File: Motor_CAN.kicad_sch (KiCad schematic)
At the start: 20 parts, among them J20 MotorCANConnector, J27 CAN_TP, J5 M_CAN_IN, J7 M_CAN_OUT, U14 ADM3055E, U15 CDSOT23-T24CAN

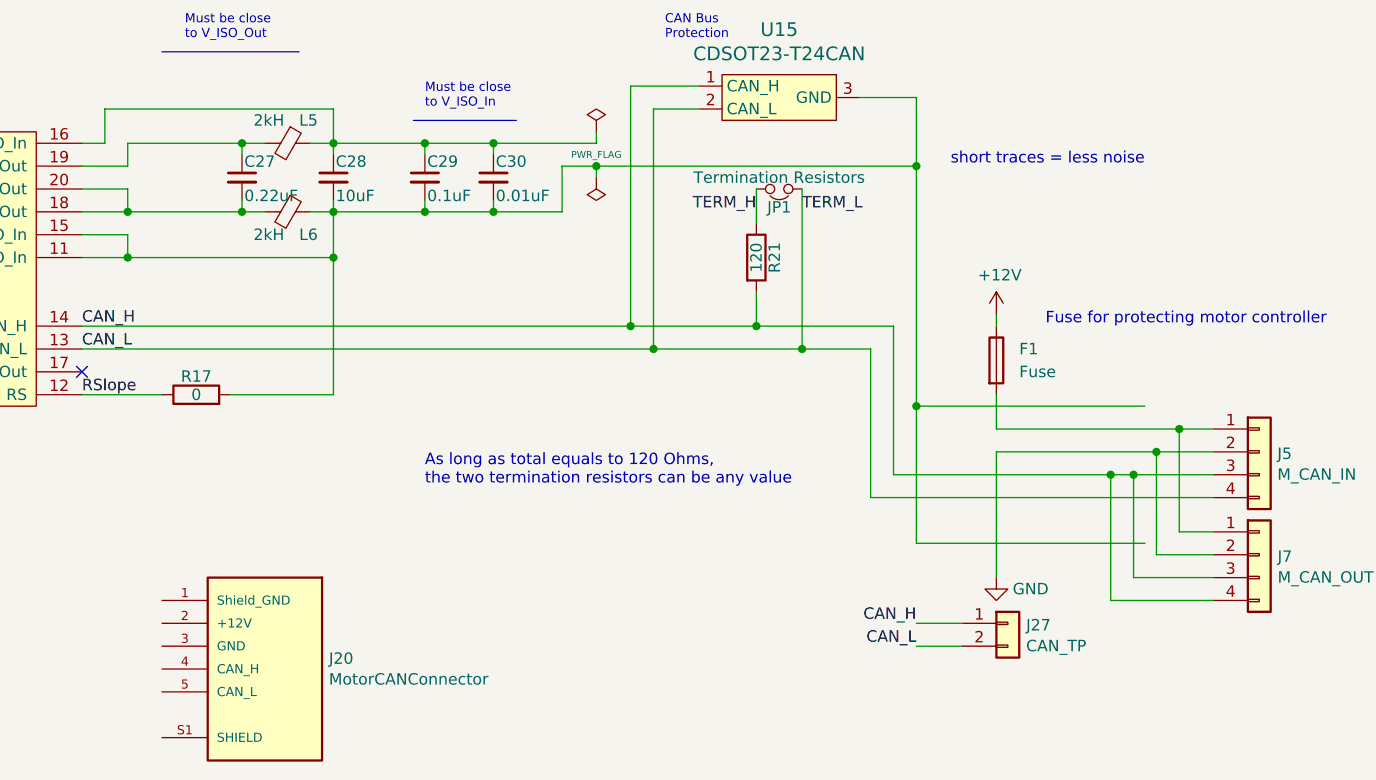
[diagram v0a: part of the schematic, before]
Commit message: Changed names and added power flags until KiCAD ERC was satisfied. Hopefully this did not involve doing anything that wasn't supposed to be done.
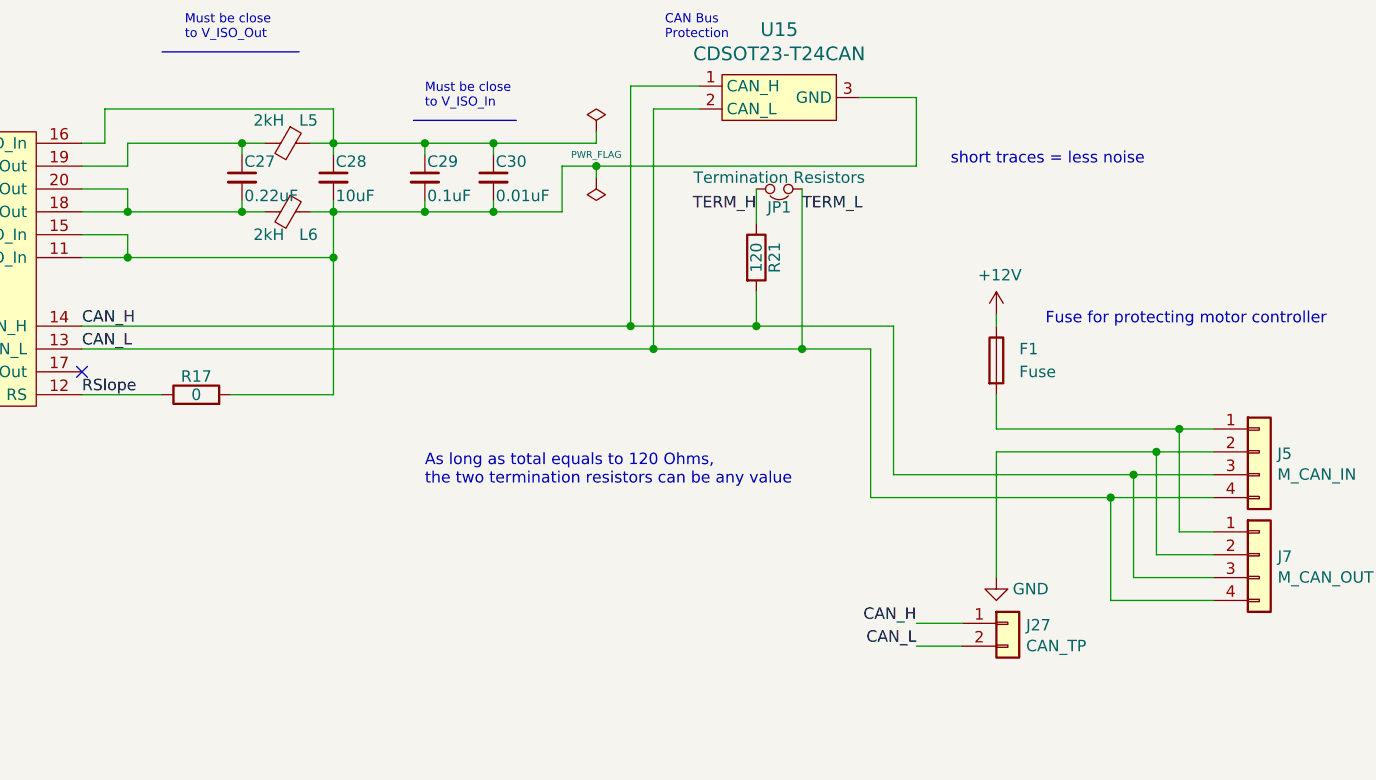
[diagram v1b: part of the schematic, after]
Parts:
- removed J20: MotorCANConnector, UTSVT_Connectors:TE_4-2172079-2, symbol Dashboard:MotorCANConnector-utsvt-connectors
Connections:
- net CAN_H: no longer J7.4 (Pin_4)
- net CAN_L: now also J7.4 (Pin_4)
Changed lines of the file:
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@@
 	)
 	(junction
-		(at 219.71 83.82)
+		(at 241.3 120.65)
 		(diameter 0)
 		(color 0 0 0 0)
@@
 	)
 	(junction
-		(at 241.3 118.11)
-		(diameter 0)
-		(color 0 0 0 0)
-	)
-	(junction
 		(at 154.94 93.98)
 		(diameter 0)
@@
 	)
 	(junction
-		(at 219.71 110.49)
-		(diameter 0)
-		(color 0 0 0 0)
-	)
-	(junction
 		(at 187.96 101.6)
 		(diameter 0)
@@
 	(wire
 		(pts
+			(xy 241.3 120.65) (xy 252.73 120.65)
+		)
+		(stroke
+			(width 0)
+			(type default)
+		)
+	)
+	(wire
+		(pts
 			(xy 187.96 101.6) (xy 201.93 101.6)
 		)
@@
 	(wire
 		(pts
-			(xy 219.71 110.49) (xy 245.11 110.49)
-		)
-		(stroke
-			(width 0)
-			(type default)
-		)
-	)
-	(wire
-		(pts
 			(xy 246.38 115.57) (xy 252.73 115.57)
 		)
@@
 		)
 	)
-	(wire
-		(pts
-			(xy 219.71 125.73) (xy 245.11 125.73)
-		)
-		(stroke
-			(width 0)
-			(type default)
-		)
-	)
 	(polyline
 		(pts
@@
 	(wire
 		(pts
-			(xy 219.71 83.82) (xy 219.71 110.49)
-		)
-		(stroke
-			(width 0)
-			(type default)
-		)
-	)
-	(wire
-		(pts
 			(xy 228.6 109.22) (xy 228.6 113.03)
 		)
@@
 	(wire
 		(pts
-			(xy 217.17 118.11) (xy 241.3 118.11)
+			(xy 217.17 118.11) (xy 243.84 118.11)
 		)
 		(stroke
@@
 	(wire
 		(pts
-			(xy 241.3 118.11) (xy 243.84 118.11)
-		)
-		(stroke
-			(width 0)
-			(type default)
-		)
-	)
-	(wire
-		(pts
 			(xy 154.94 77.47) (xy 154.94 81.28)
 		)
@@
 	(wire
 		(pts
+			(xy 241.3 120.65) (xy 241.3 132.08)
+		)
+		(stroke
+			(width 0)
+			(type default)
+		)
+	)
+	(wire
+		(pts
 			(xy 90.17 92.71) (xy 91.44 92.71)
 		)
@@
 	(wire
 		(pts
-			(xy 241.3 132.08) (xy 241.3 118.11)
-		)
-		(stroke
-			(width 0)
-			(type default)
-		)
-	)
-	(wire
-		(pts
 			(xy 82.55 85.09) (xy 82.55 86.36)
 		)
@@
 	(wire
 		(pts
-			(xy 219.71 110.49) (xy 219.71 125.73)
-		)
-		(stroke
-			(width 0)
-			(type default)
-		)
-	)
-	(wire
-		(pts
 			(xy 132.08 93.98) (xy 154.94 93.98)
 		)
@@
 	(wire
 		(pts
-			(xy 214.63 120.65) (xy 252.73 120.65)
+			(xy 214.63 120.65) (xy 241.3 120.65)
 		)
 		(stroke
@@
 					(unit 1)
 				)
-			)
-		)
-	)
-	(symbol
-		(lib_id "Dashboard:MotorCANConnector-utsvt-connectors")
-		(at 143.51 152.4 0)
-		(mirror y)
-		(unit 1)
-		(exclude_from_sim no)
-		(in_bom yes)
-		(on_board yes)
-		(dnp no)
-		(property "Reference" "J20"
-			(at 154.432 138.5316 0)
-			(effects
-				(font
-					(size 1.27 1.27)
-				)
-				(justify right)
-			)
-		)
-		(property "Value" "MotorCANConnector"
-			(at 154.432 140.843 0)
-			(effects
-				(font
-					(size 1.27 1.27)
-				)
-				(justify right)
-			)
-		)
-		(property "Footprint" "UTSVT_Connectors:TE_4-2172079-2"
-			(at 143.51 152.4 0)
-			(effects
-				(font
-					(size 1.27 1.27)
-				)
-				(hide yes)
-			)
-		)
-		(property "Datasheet" ""
-			(at 143.51 152.4 0)
-			(effects
-				(font
-					(size 1.27 1.27)
-				)
-				(hide yes)
-			)
-		)
-		(property "Description" ""
-			(at 143.51 152.4 0)
-			(effects
-				(font
-					(size 1.27 1.27)
-				)
-				(hide yes)
-			)
-		)
-		(property "Digikey" "https://www.digikey.com/product-detail/en/te-connectivity-amp-connectors/4-2172079-2/A120861-ND/5118755"
-			(at 143.51 152.4 0)
-			(effects
-				(font
-					(size 1.27 1.27)
-				)
-				(hide yes)
-			)
-		)
-		(pin "1"
-		)
-		(pin "2"
-		)
-		(pin "3"
-		)
-		(pin "4"
-		)
-		(pin "5"
-		)
-		(pin "S1"
-		)
-		(instances
-			(project "Controls-Leader"
-				(path "/66218487-e316-4467-9eba-79d4626ab24e/00000000-0000-0000-0000-00005f6018fb"
-					(reference "J20")
-					(unit 1)
-				)

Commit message: Fuse footprint added and blinker changed to software
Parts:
- F1: footprint (none) -> Fuse:Fuse_1206_3216Metric
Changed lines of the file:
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@@
 			)
 		)
-		(property "Footprint" ""
+		(property "Footprint" "Fuse:Fuse_1206_3216Metric"
 			(at 226.822 105.41 90)
 			(effects
@@
 			)
 		)
-		(property "Datasheet" "~"
+		(property "Datasheet" "https://www.littelfuse.com/~/media/electronics/datasheets/fuses/littelfuse_fuse_437_datasheet.pdf.pdf"
 			(at 228.6 105.41 0)
 			(effects

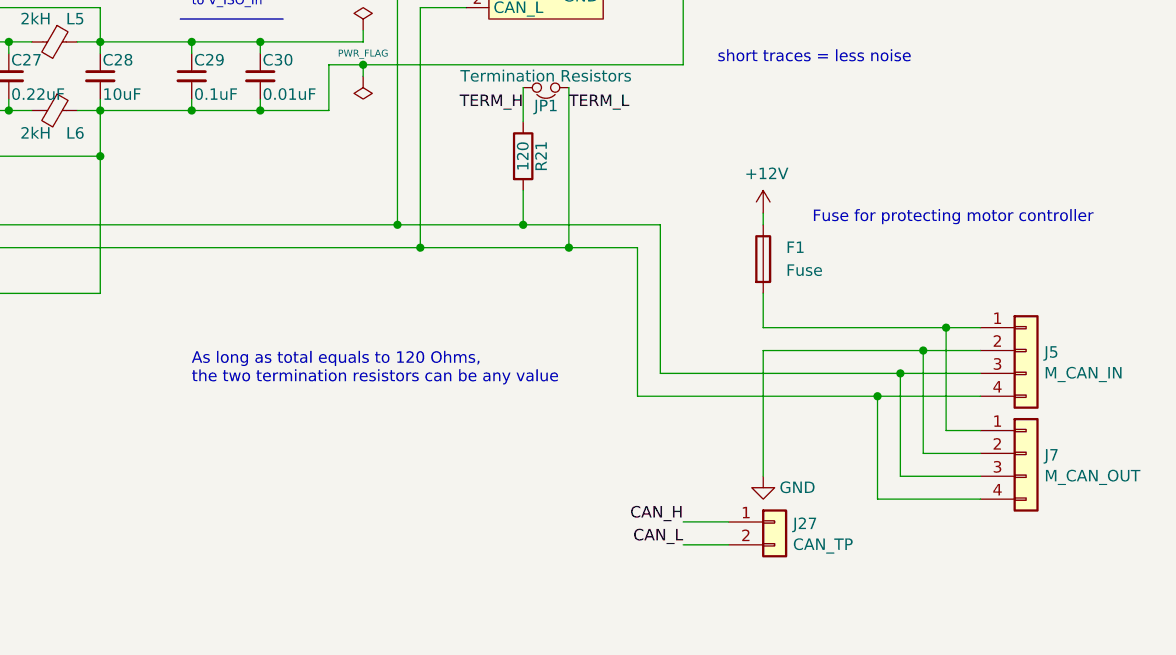
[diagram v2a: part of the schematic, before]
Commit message: Started cleaning some comments, changed EL3H7 data sheet link, removed extra motor CAN connector and changed original one to match (I think) motor controller connector, removed extra mounting holes, removed hierarchical power labels.
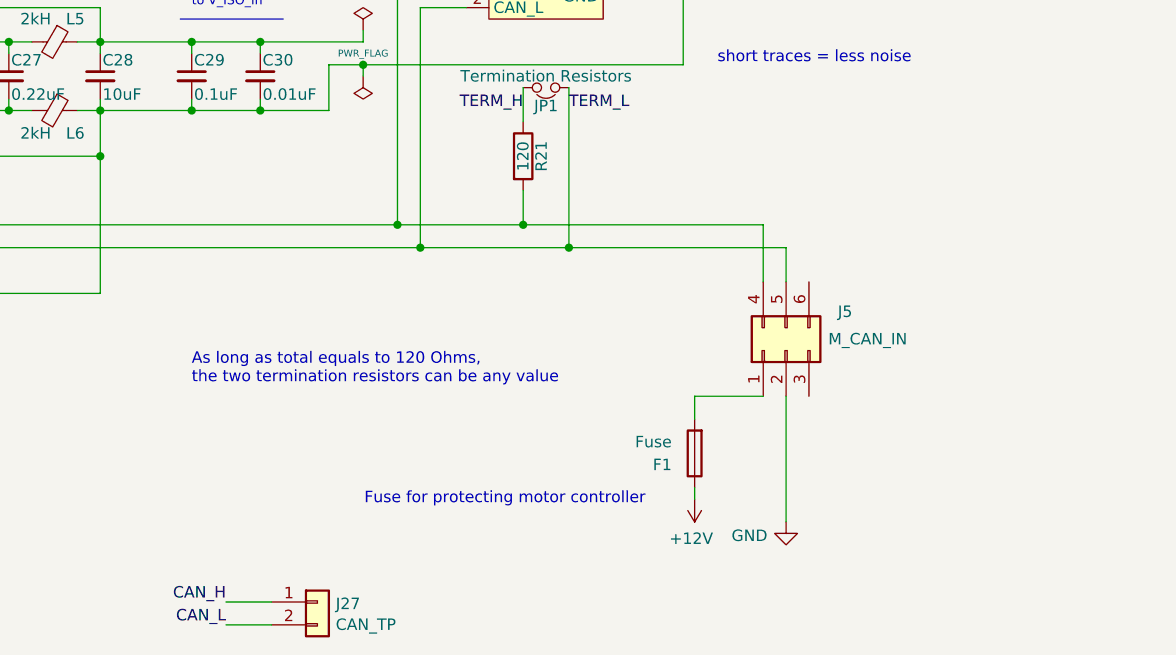
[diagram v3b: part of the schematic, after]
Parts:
- removed J7: M_CAN_OUT, UTSVT_Connectors:Molex_MicroFit3.0_1x4xP3.00mm_PolarizingPeg_Vertical, symbol Connector_Generic:Conn_01x04
- J5: footprint UTSVT_Connectors:Molex_MicroFit3.0_1x4xP3.00mm_PolarizingPeg_Vertical -> Connector_Molex:Molex_Micro-Fit_3.0_43045-0612_2x03_P3.00mm_Vertical; symbol Connector_Generic:Conn_01x04 -> Connector_Generic:Conn_02x03_Top_Bottom
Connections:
- net CAN_H: now also J5.4 (Pin_4); no longer J5.3 (Pin_3)
- net CAN_L: now also J5.5 (Pin_5); no longer J5.4 (Pin_4)
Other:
- moved on the sheet: F1, J27

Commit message: fixed some footprints and part numbers
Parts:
- F1: Mouser Part Number (none) -> 576-0440.375WR
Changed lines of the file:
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@@
+			)
+		)
+		(property "Mouser Part Number" "576-0440.375WR"
+			(at 220.98 127 0)
+			(effects
+				(font
+					(size 1.27 1.27)
+				)
+				(hide yes)
 			)
 		)

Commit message: Added/checked datasheet links/part numbers, deleted accel_pot2 and brake_pot2 hierarchical labels and changed corresponding pins (PC2, PC3) to GPIO on the now-2x5 extra GPIO connector.
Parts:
- C23, C28: Mouser Part Number 80-C0805C106K8RAUTO -> 963-TMK212BBJ106MGHT
- C24, C25, C29: Mouser Part Number 80-C0805C104K3R -> 80-C0805C104M5R
- C26, C30: Mouser Part Number 80-C0805X103K1R3316 -> C0805C103J5RACTU
- C27: Mouser Part Number 80-C0805C224J1RECTU -> 80-C0805C224J1RECTU
- R21: Mouser Part Number 71-CRCW080559R0FKEA -> CRCW0805120RFKEA
- U14: P/N (none) -> ADM3055E
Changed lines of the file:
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@@
 			)
 		)
-		(property "Datasheet" "~"
+		(property "Datasheet" "https://www.mouser.com/ProductDetail/71-CRCW0805120RFKEA"
 			(at 201.93 93.98 0)
 			(effects
@@
 			)
 		)
-		(property "Mouser Part Number" "71-CRCW080559R0FKEA"
+		(property "Mouser Part Number" "CRCW0805120RFKEA"
 			(at 201.93 93.98 0)
 			(effects
@@
 			)
 		)
-		(property "Datasheet" "~"
+		(property "Datasheet" "https://www.mouser.com/ProductDetail/TAIYO-YUDEN/TMK212BBJ106MGHT?qs=sGAEpiMZZMsh%252B1woXyUXj6Ion9DcW8uk%2FCsbgn7gICc%3D"
 			(at 53.34 88.9 0)
 			(effects
@@
 			)
 		)
-		(property "Mouser Part Number" "80-C0805C106K8RAUTO "
+		(property "Mouser Part Number" "963-TMK212BBJ106MGHT"
 			(at 53.34 88.9 0)
 			(effects
@@
 			)
 		)
-		(property "Datasheet" "~"
+		(property "Datasheet" "https://www.mouser.com/ProductDetail/KEMET/C0805C104M5RACTU?qs=VOOUd%252Bza08qHu13WgNByHQ%3D%3D"
 			(at 62.23 88.9 0)
 			(effects
@@
 			)
 		)
-		(property "Mouser Part Number" "80-C0805C104K3R "
+		(property "Mouser Part Number" "80-C0805C104M5R"
 			(at 62.23 88.9 0)
 			(effects
@@
 			)
 		)
-		(property "Datasheet" "~"
+		(property "Datasheet" "https://www.mouser.com/ProductDetail/KEMET/C0805C104M5RACTU?qs=VOOUd%252Bza08qHu13WgNByHQ%3D%3D"
 			(at 73.66 88.9 0)
 			(effects
@@
 			)
 		)
-		(property "Mouser Part Number" "80-C0805C104K3R "
+		(property "Mouser Part Number" "80-C0805C104M5R"
 			(at 73.66 88.9 0)
 			(effects
@@
 			)
 		)
-		(property "Datasheet" "~"
+		(property "Datasheet" "https://www.mouser.com/ProductDetail/KEMET/C0805C103J5RACTU?qs=Onq5MIl0ZjiJ615hCkQQ7A%3D%3D"
 			(at 82.55 88.9 0)
 			(effects
@@
 			)
 		)
-		(property "Mouser Part Number" "80-C0805X103K1R3316 "
+		(property "Mouser Part Number" "C0805C103J5RACTU"
 			(at 82.55 88.9 0)
 			(effects
@@
 			)
 		)
-		(property "Datasheet" "~"
+		(property "Datasheet" "https://www.mouser.com/ProductDetail/TAIYO-YUDEN/TMK212BBJ106MGHT?qs=sGAEpiMZZMsh%252B1woXyUXj6Ion9DcW8uk%2FCsbgn7gICc%3D"
 			(at 154.94 85.09 0)
 			(effects
@@
 			)
 		)
-		(property "Mouser Part Number" "80-C0805C106K8RAUTO "
+		(property "Mouser Part Number" "963-TMK212BBJ106MGHT"
 			(at 154.94 85.09 0)
 			(effects
@@
 			)
 		)
-		(property "Datasheet" "~"
+		(property "Datasheet" "https://www.mouser.com/ProductDetail/KEMET/C0805C224J1RECTU?qs=55YtniHzbhA8coEmCgZh4A%3D%3D&srsltid=AfmBOope8E98p1TAxytK4MEkGo55JjU107N1pzX-xa8_vzbWYaq6BWq_"
 			(at 144.78 85.09 0)
 			(effects
@@
 			)
 		)
-		(property "Mouser Part Number" "80-C0805C224J1RECTU "
+		(property "Mouser Part Number" "80-C0805C224J1RECTU"
 			(at 144.78 85.09 0)
 			(effects
@@
 			)
 		)
-		(property "Datasheet" ""
+		(property "Datasheet" "https://www.mouser.com/ProductDetail/TAIYO-YUDEN/BK2125LM182-T?qs=I6KAKw0tg2wTd%252Bj343lu1Q%3D%3D&srsltid=AfmBOorkhsm8Uk29brVkfBS5oJy8t8TPSw1gIhtEERu0OY8r33ydtYfJ"
 			(at 149.86 81.28 0)
 			(effects
@@
 			)
 		)
-		(property "Datasheet" ""
+		(property "Datasheet" "https://www.mouser.com/ProductDetail/TAIYO-YUDEN/BK2125LM182-T?qs=I6KAKw0tg2wTd%252Bj343lu1Q%3D%3D&srsltid=AfmBOorkhsm8Uk29brVkfBS5oJy8t8TPSw1gIhtEERu0OY8r33ydtYfJ"
 			(at 149.86 88.9 0)
 			(effects
@@
 			)
 		)
-		(property "Datasheet" "~"
+		(property "Datasheet" "https://www.mouser.com/ProductDetail/KEMET/C0805C104M5RACTU?qs=VOOUd%252Bza08qHu13WgNByHQ%3D%3D"
 			(at 165.1 85.09 0)
 			(effects
@@
 			)
 		)
-		(property "Mouser Part Number" "80-C0805C104K3R "
+		(property "Mouser Part Number" "80-C0805C104M5R"
 			(at 165.1 85.09 0)
 			(effects
@@
 			)
 		)
-		(property "Datasheet" "~"
+		(property "Datasheet" "https://www.mouser.com/ProductDetail/KEMET/C0805C103J5RACTU?qs=Onq5MIl0ZjiJ615hCkQQ7A%3D%3D"
 			(at 172.72 85.09 0)
 			(effects
@@
 			)
 		)
-		(property "Mouser Part Number" "80-C0805X103K1R3316 "
+		(property "Mouser Part Number" "C0805C103J5RACTU"
 			(at 172.72 85.09 0)
 			(effects
@@
 			)
 		)
-		(property "Datasheet" "~"
+		(property "Datasheet" "https://www.mouser.in/ProductDetail/Vishay-Dale/CRCW08050000Z0EAC?qs=E3Y5ESvWgWMnvHb9ZvShmA%3D%3D"
 			(at 139.7 109.22 0)
 			(effects
@@
 			(at 109.22 95.25 0)
 			(effects
+				(font
+					(size 1.27 1.27)
+				)
+				(hide yes)
+			)
+		)
+		(property "P/N" "ADM3055E"
+			(at 109.22 95.25 0)
+			(effects

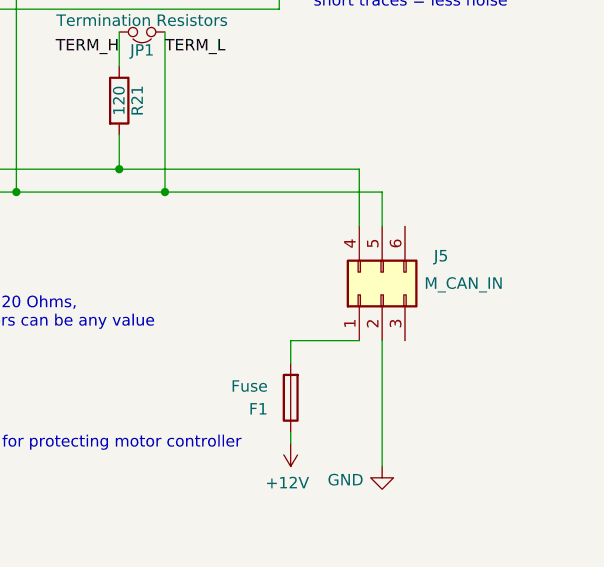
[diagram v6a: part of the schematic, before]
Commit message: Forgot to save, so this might include some changes from the last commit with the deleted potentiometer pins. Also added no-connects to shield pins of motor can.
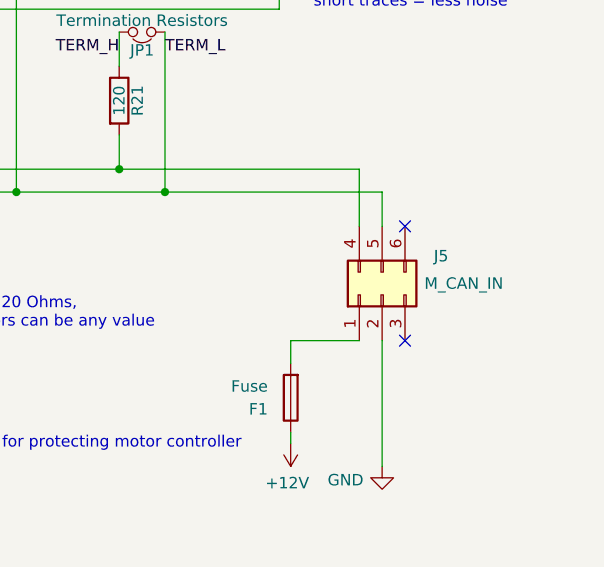
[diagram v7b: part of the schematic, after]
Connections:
- no-connect marks 4 -> 6
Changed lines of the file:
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@@
+	)
+	(no_connect
+		(at 233.68 120.65)
 	)
 	(no_connect
 		(at 91.44 105.41)
 	)
+	(no_connect
+		(at 233.68 107.95)
+	)
 	(wire

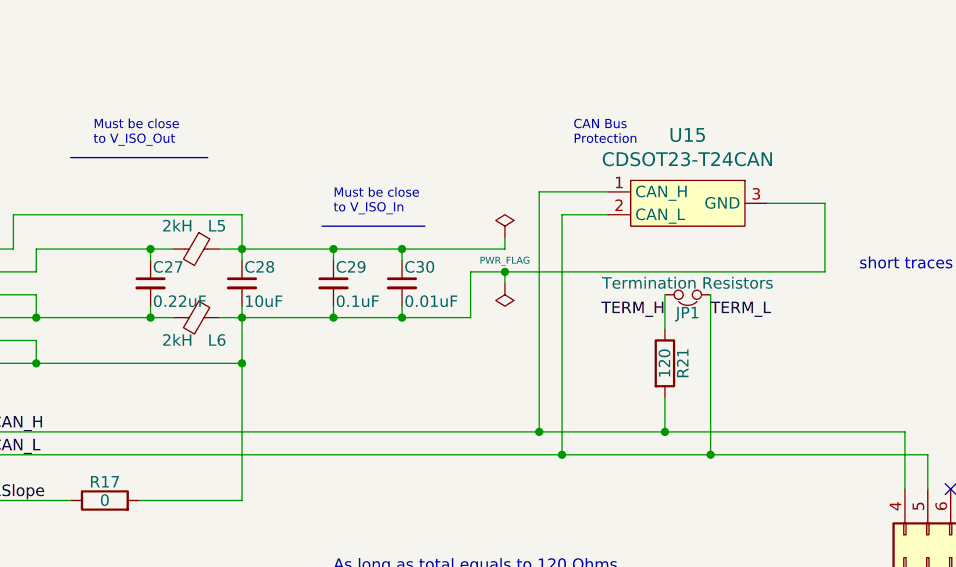
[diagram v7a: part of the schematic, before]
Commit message: Updated ferrite beads.
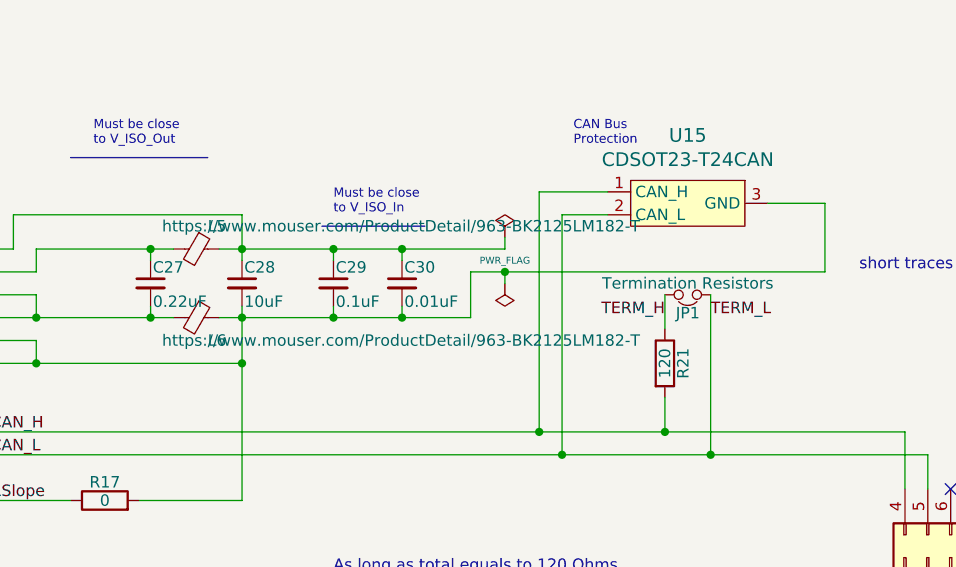
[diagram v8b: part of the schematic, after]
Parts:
- L5, L6: value 2kH -> https://www.mouser.com/ProductDetail/963-BK2125LM182-T; Mouser Part Number 963-BK2125LM182-T -> BKH1005LM182-T
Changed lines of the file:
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@@
 			)
 		)
-		(property "Value" "2kH"
+		(property "Value" "https://www.mouser.com/ProductDetail/963-BK2125LM182-T"
 			(at 146.05 78.74 90)
 			(effects
@@
 			)
 		)
-		(property "Mouser Part Number" "963-BK2125LM182-T "
+		(property "Mouser Part Number" "BKH1005LM182-T "
 			(at 149.86 81.28 0)
 			(effects
@@
 			)
 		)
-		(property "Value" "2kH"
+		(property "Value" "https://www.mouser.com/ProductDetail/963-BK2125LM182-T"
 			(at 146.05 91.44 90)
 			(effects
@@
 			)
 		)
-		(property "Mouser Part Number" "963-BK2125LM182-T "
+		(property "Mouser Part Number" "BKH1005LM182-T "
 			(at 149.86 88.9 0)
 			(effects
